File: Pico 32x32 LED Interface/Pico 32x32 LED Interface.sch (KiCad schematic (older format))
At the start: 2 parts, among them J1001 Conn_01x20_Female, U1001 SN74LVC4245APWR

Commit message: Working on things...
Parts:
- removed J1001: Conn_01x20_Female, Connector_PinHeader_2.54mm:PinHeader_1x20_P2.54mm_Vertical, symbol Connector:Conn_01x20_Female
- added C1001, C1002: 100n, Capacitor_SMD:C_0402_1005Metric, symbol Device:C
- added J1002: Conn_02x08_Odd_Even, Connector_PinHeader_2.54mm:PinHeader_2x08_P2.54mm_Vertical, symbol Connector_Generic:Conn_02x08_Odd_Even
- added U?: Pico_Header, symbol LevelShifter:Pico_Header
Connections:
- net +5V: now reaches U1001.1 (VCCA)
- net +5V: now also C1001.1
- net GND: now reaches U1001.11 (GND)
- net GND: now also U1001.12 (GND), U1001.13 (GND), U1001.2 (DIR), U1001.22 (~OE), C1001.2, C1002.1, J1002.16 (Pin_16), J1002.4 (Pin_4), J1002.8 (Pin_8)
- net +3V3: now reaches U1001.23 (VCCB)
- net +3V3: now also U1001.24 (VCCB), C1002.2
- new net AOut: J1002.9 (Pin_9)
- new net B1Out: J1002.3 (Pin_3)
- new net B2Out: J1002.7 (Pin_7)
- new net BOut: J1002.10 (Pin_10)
- new net CLK: J1002.13 (Pin_13)
- new net COut: J1002.11 (Pin_11)
- new net DOut: J1002.12 (Pin_12)
- new net G1Out: J1002.2 (Pin_2)
- new net G2Out: J1002.6 (Pin_6)
- new net LatchOut: J1002.14 (Pin_14)
- new net R1Out: J1002.1 (Pin_1)
- new net R2Out: J1002.5 (Pin_5)
- new net ~OEOut: J1002.15 (Pin_15)

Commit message: Finishing draft
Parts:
- added C2, C4: 100n, Capacitor_SMD:C_0402_1005Metric, symbol Device:C
- added U2: SN74LVC4245APWR, Package_SO:TSSOP-24_6.1x7.8mm_P0.65mm, symbol LevelShifter:SN74LVC4245APWR
- U3: renamed from U?; footprint (none) -> Pico 32x32 LED Interface:Pico_In_Headers
- renumbered C1001 to C1, C1002 to C3, J1002 to J1, U1001 to U1
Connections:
- net CLK is gone; now on net CLKOut: J1.13 (Pin_13)
- net +3V3: now also U3.36 (3V3), C4.2, U2.23 (VCCB), U2.24 (VCCB)
- net +5V: now also U3.40 (VBUS), C2.1, U2.1 (VCCA)
- net AOut: now also U2.6 (A4)
- net B1Out: now also U1.7 (A5)
- net B2Out: now also U1.5 (A3)
- net BOut: now also U2.5 (A3)
- net COut: now also U2.8 (A6)
- net DOut: now also U2.7 (A5)
- net G1Out: now also U1.9 (A7)
- net G2Out: now also U1.10 (A8)
- net GND: now also U3.13 (GND), U3.18 (GND), U3.23 (GND), U3.28 (GND), U3.3 (GND), U3.33 (GND), U3.38 (GND), U3.8 (GND), C2.2, C4.1, U2.11 (GND), U2.12 (GND), U2.13 (GND), U2.14 (B8), U2.15 (B7), U2.2 (DIR), U2.21 (B1), U2.22 (~OE)
- net LatchOut: now also U1.4 (A2)
- net R1Out: now also U1.8 (A6)
- net R2Out: now also U1.6 (A4)
- net ~OEOut: now also U2.4 (A2)
- net at U3.1 (GP0): now also U1.21 (B1)
- net at U3.10 (GP7): now also U1.14 (B8)
- net at U3.11 (GP8): now also U2.20 (B2)
- net at U3.12 (GP9): now also U2.19 (B3)
- net at U3.14 (GP10): now also U2.18 (B4)
- net at U3.15 (GP11): now also U2.17 (B5)
- net at U3.16 (GP12): now also U2.16 (B6)
- net at U3.2 (GP1): now also U1.20 (B2)
- net at U3.4 (GP2): now also U1.19 (B3)
- net at U3.5 (GP3): now also U1.18 (B4)
- net at U3.6 (GP4): now also U1.17 (B5)
- net at U3.7 (GP5): now also U1.16 (B6)
- net at U3.9 (GP6): now also U1.15 (B7)
- net CLKOut: now reaches U1.3 (A1)
- no-connect marks 0 -> 20
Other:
- moved on the sheet: C1, C3, U1, U3

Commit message: Fixing TSSOP footprints (#9)
Fixes the footprints of the TSSOP packages, after JLCPCB caught the error.

Since order, I've noticed two more issues:
- The decoupling capacitors may need larger footprints too (there was a warning about them, but JLCPCB didn't message me like they did for the TSSOP footprints)
- The pinout from the Pico needs to change. I've been learning about the differences between `out`, `set` and `sideset` pins since the order went into production
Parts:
- U1, U2: footprint Package_SO:TSSOP-24_6.1x7.8mm_P0.65mm -> Package_SO:TSSOP-24_4.4x7.8mm_P0.65mm
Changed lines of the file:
@@
 F 0 "U1" H 4900 3855 50  0000 C CNN
 F 1 "SN74LVC4245APWR" H 4900 3764 50  0000 C CNN
-F 2 "Package_SO:TSSOP-24_6.1x7.8mm_P0.65mm" H 4900 2750 50  0001 C CNN
+F 2 "Package_SO:TSSOP-24_4.4x7.8mm_P0.65mm" H 4900 2750 50  0001 C CNN
 F 3 "https://datasheet.lcsc.com/lcsc/1809192324_Texas-Instruments-SN74LVC4245APWR_C7859.pdf" H 4900 2750 50  0001 C CNN
 F 4 "C7859" H 4900 3673 50  0000 C CNN "LCSC"
@@
 F 0 "U2" H 4900 6505 50  0000 C CNN
 F 1 "SN74LVC4245APWR" H 4900 6414 50  0000 C CNN
-F 2 "Package_SO:TSSOP-24_6.1x7.8mm_P0.65mm" H 4900 5400 50  0001 C CNN
+F 2 "Package_SO:TSSOP-24_4.4x7.8mm_P0.65mm" H 4900 5400 50  0001 C CNN
 F 3 "https://datasheet.lcsc.com/lcsc/1809192324_Texas-Instruments-SN74LVC4245APWR_C7859.pdf" H 4900 5400 50  0001 C CNN
 F 4 "C7859" H 4900 6323 50  0000 C CNN "LCSC"

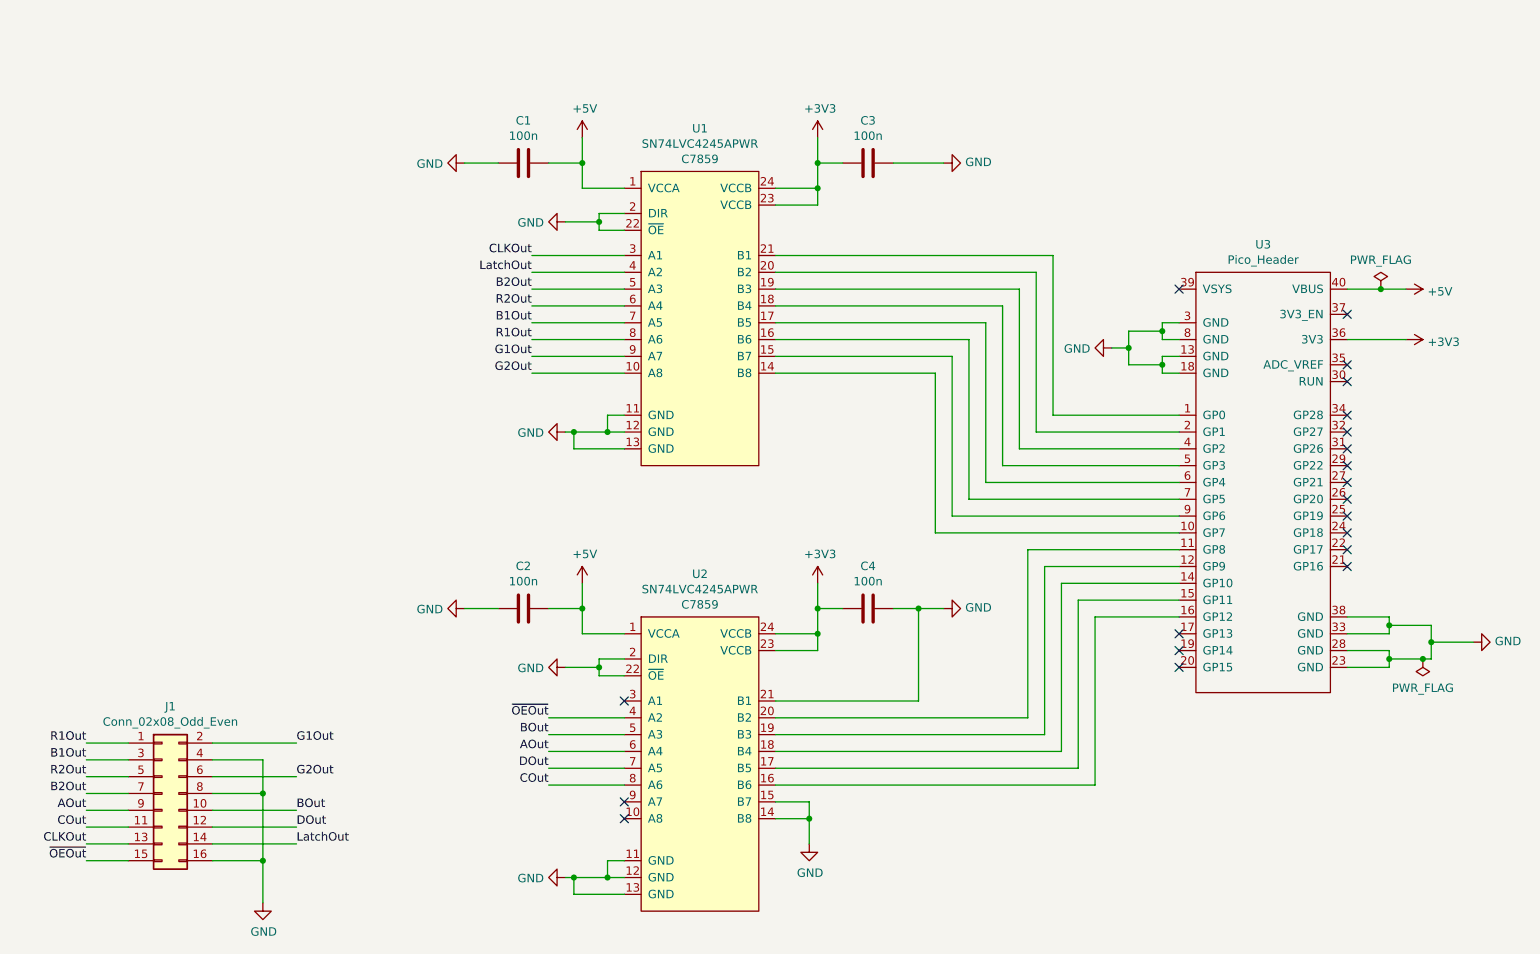
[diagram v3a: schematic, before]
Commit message: Working on reordering connections
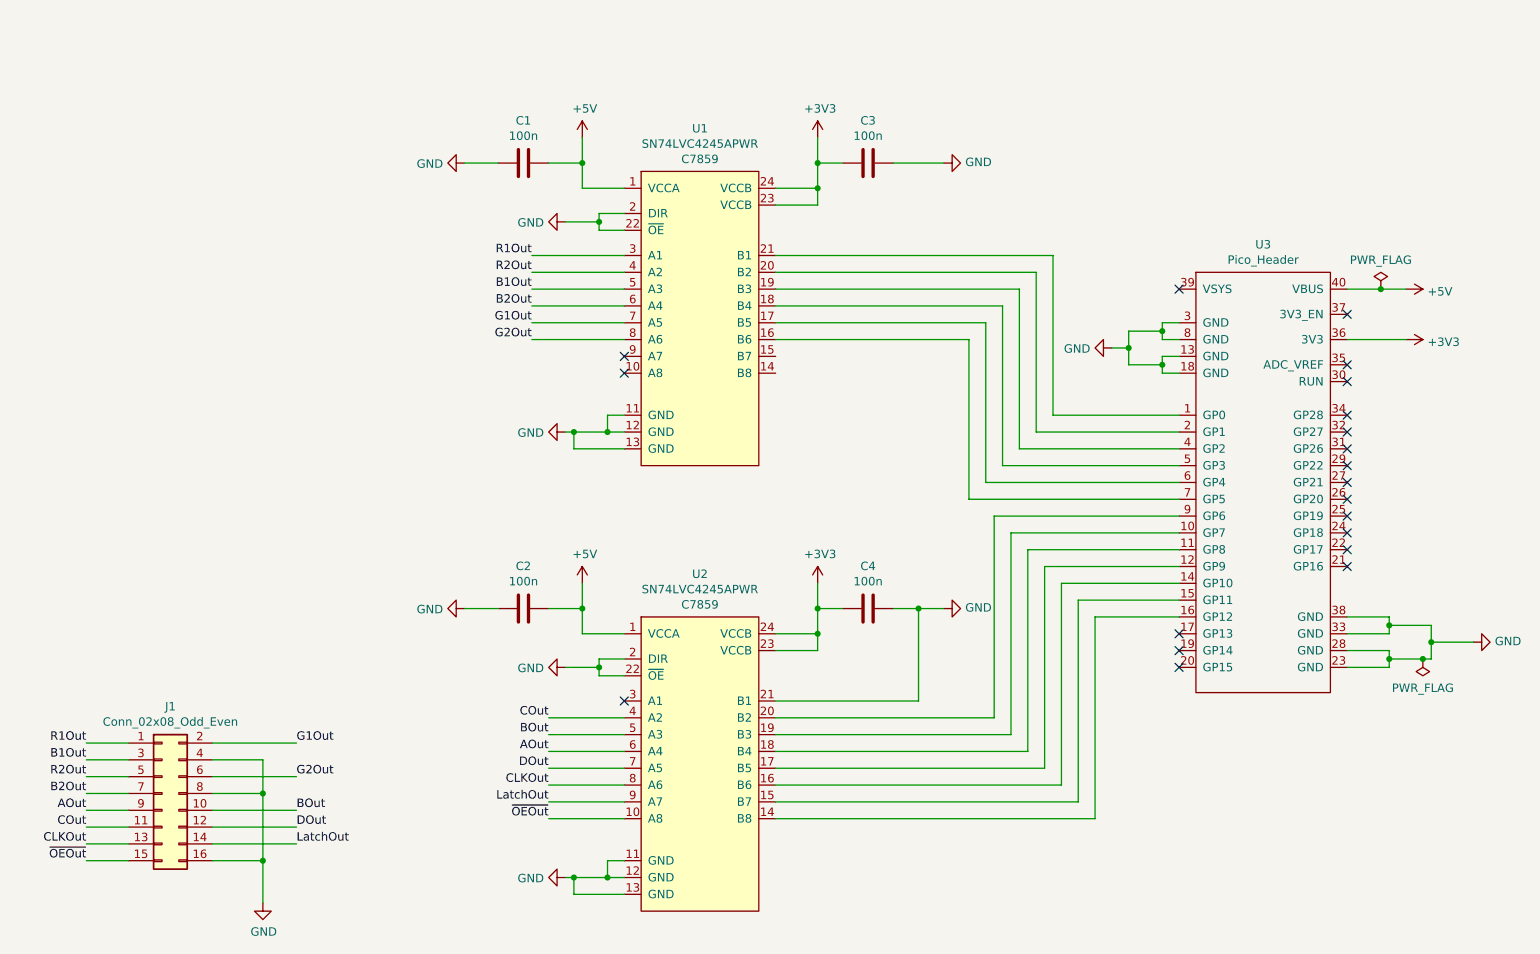
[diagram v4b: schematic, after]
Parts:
- C2, C4: footprint Capacitor_SMD:C_0402_1005Metric -> Capacitor_SMD:C_0402_1005Metric_Pad0.74x0.62mm_HandSolder
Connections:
- net B1Out: now also U1.5 (A3); no longer U1.7 (A5)
- net B2Out: now also U1.6 (A4); no longer U1.5 (A3)
- net CLKOut: now also U2.8 (A6); no longer U1.3 (A1)
- net COut: now also U2.4 (A2); no longer U2.8 (A6)
- net G1Out: now also U1.7 (A5); no longer U1.9 (A7)
- net G2Out: now also U1.8 (A6); no longer U1.10 (A8)
- net GND: no longer U2.14 (B8), U2.15 (B7)
- net LatchOut: now also U2.9 (A7); no longer U1.4 (A2)
- net R1Out: now also U1.3 (A1); no longer U1.8 (A6)
- net R2Out: now also U1.4 (A2); no longer U1.6 (A4)
- net ~OEOut: now also U2.10 (A8); no longer U2.4 (A2)
- net at U3.10 (GP7): now also U2.19 (B3); no longer U1.14 (B8)
- net at U3.11 (GP8): now also U2.18 (B4); no longer U2.20 (B2)
- net at U3.12 (GP9): now also U2.17 (B5); no longer U2.19 (B3)
- net at U3.14 (GP10): now also U2.16 (B6); no longer U2.18 (B4)
- net at U3.15 (GP11): now also U2.15 (B7); no longer U2.17 (B5)
- net at U3.16 (GP12): now also U2.14 (B8); no longer U2.16 (B6)
- net at U3.9 (GP6): now also U2.20 (B2); no longer U1.15 (B7)
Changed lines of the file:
@@
 F 0 "C2" V 3598 4500 50  0000 C CNN
 F 1 "100n" V 3689 4500 50  0000 C CNN
-F 2 "Capacitor_SMD:C_0402_1005Metric" H 3888 4350 50  0001 C CNN
+F 2 "Capacitor_SMD:C_0402_1005Metric_Pad0.74x0.62mm_HandSolder" H 3888 4350 50  0001 C CNN
 F 3 "~" H 3850 4500 50  0001 C CNN
 F 4 "C1525" H 3850 4500 50  0001 C CNN "LCSC"
@@
 F 0 "C4" V 5648 4500 50  0000 C CNN
 F 1 "100n" V 5739 4500 50  0000 C CNN
-F 2 "Capacitor_SMD:C_0402_1005Metric" H 5938 4350 50  0001 C CNN
+F 2 "Capacitor_SMD:C_0402_1005Metric_Pad0.74x0.62mm_HandSolder" H 5938 4350 50  0001 C CNN
 F 3 "~" H 5900 4500 50  0001 C CNN
 F 4 "C1525" H 5900 4500 50  0001 C CNN "LCSC"
@@
 Wire Wire Line
 	6500 3850 7750 3850
-Wire Wire Line
-	5350 3000 6400 3000
-Wire Wire Line
-	6400 3000 6400 3950
-Wire Wire Line
-	6400 3950 7750 3950
 Text Label 3900 2400 2    50   ~ 0
-CLKOut
+R1Out
 Wire Wire Line
 	3900 2400 4450 2400
 Wire Wire Line
-	5350 5150 6850 5150
-Wire Wire Line
-	6850 5150 6850 4150
-Wire Wire Line
 	6850 4150 7750 4150
 Wire Wire Line
-	5350 5250 6950 5250
-Wire Wire Line
-	6950 5250 6950 4250
-Wire Wire Line
 	6950 4250 7750 4250
 Wire Wire Line
-	5350 5350 7050 5350
-Wire Wire Line
-	7050 5350 7050 4350
-Wire Wire Line
 	7050 4350 7750 4350
 Wire Wire Line
 	7750 4450 7150 4450
 Wire Wire Line
-	7150 4450 7150 5450
-Wire Wire Line
-	7150 5450 5350 5450
-Wire Wire Line
-	5350 5550 7250 5550
-Wire Wire Line
-	7250 5550 7250 4550
-Wire Wire Line
 	7250 4550 7750 4550
-$Comp
-L power:GND #PWR0101
-U 1 1 619DC3E4
-P 5550 5900
-F 0 "#PWR0101" H 5550 5650 50  0001 C CNN
-F 1 "GND" H 5555 5727 50  0000 C CNN
-F 2 "" H 5550 5900 50  0001 C CNN
-F 3 "" H 5550 5900 50  0001 C CNN
-	1    5550 5900
-	1    0    0    -1
-$EndComp
-Wire Wire Line
-	5350 5650 5550 5650
-Wire Wire Line
-	5550 5650 5550 5750
-Connection ~ 5550 5750
-Wire Wire Line
-	5550 5750 5550 5900
-Wire Wire Line
-	5350 5750 5550 5750
 Text Label 3900 2500 2    50   ~ 0
-LatchOut
+R2Out
 Wire Wire Line
 	3900 2500 4450 2500
 Text Label 3900 2600 2    50   ~ 0
-B2Out
+B1Out
 Wire Wire Line
 	3900 2600 4450 2600
 Text Label 3900 2700 2    50   ~ 0
-R2Out
+B2Out
 Text Label 3900 2800 2    50   ~ 0
-B1Out
+G1Out
 Wire Wire Line
 	3900 2700 4450 2700
 Wire Wire Line
 	3900 2800 4450 2800
-Wire Wire Line
-	6300 3100 6300 4050
-Wire Wire Line
-	6300 4050 7750 4050
-Wire Wire Line
-	5350 3100 6300 3100
 Wire Wire Line
 	5350 5050 6200 5050
@@
 	6200 4500 6350 4500
 Text Label 3900 2900 2    50   ~ 0
-R1Out
-Text Label 3900 3000 2    50   ~ 0
-G1Out
-Text Label 3900 3100 2    50   ~ 0
 G2Out
 Wire Wire Line
 	3900 2900 4450 2900
-Wire Wire Line
-	3900 3000 4450 3000
-Wire Wire Line
-	3900 3100 4450 3100
-NoConn ~ 4450 5650
-NoConn ~ 4450 5750
-NoConn ~ 4450 5050
 Text Label 4000 5250 2    50   ~ 0
 BOut
@@
 DOut
 Text Label 4000 5550 2    50   ~ 0
+CLKOut
+Text Label 4000 5150 2    50   ~ 0
 COut
-Text Label 4000 5150 2    50   ~ 0
-~OEOut
 Wire Wire Line
 	4000 5150 4450 5150
@@
 Wire Wire Line
 	8950 2600 9100 2600
+NoConn ~ 4450 3000
+NoConn ~ 4450 3100
+Wire Wire Line
+	7750 4050 6750 4050
+Wire Wire Line
+	7750 3950 6650 3950
+Wire Wire Line
+	6650 3950 6650 5150
+Wire Wire Line
+	6650 5150 5350 5150
+Wire Wire Line
+	6750 4050 6750 5250
+Wire Wire Line
+	6750 5250 5350 5250
+Wire Wire Line
+	6850 4150 6850 5350
+Wire Wire Line
+	6850 5350 5350 5350
+Wire Wire Line
+	6950 4250 6950 5450
+Wire Wire Line
+	6950 5450 5350 5450
+Wire Wire Line
+	7050 4350 7050 5550
+Wire Wire Line
+	7050 5550 5350 5550
+Wire Wire Line
+	7150 4450 7150 5650
+Wire Wire Line
+	7150 5650 5350 5650
+Wire Wire Line
+	7250 4550 7250 5750
+Wire Wire Line
+	7250 5750 5350 5750
+Wire Wire Line
+	4450 5650 4000 5650
+Wire Wire Line
+	4450 5750 4000 5750
+Text Label 4000 5750 2    50   ~ 0
+~OEOut
+Text Label 4000 5650 2    50   ~ 0
+LatchOut
+NoConn ~ 4450 5050
 $EndSCHEMATC

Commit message: Some more routine
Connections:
- net CLKOut: now also U2.10 (A8); no longer U2.8 (A6)
- net GND: now also U1.14 (B8), U1.15 (B7)
- net LatchOut: now also U2.8 (A6); no longer U2.9 (A7)
- net ~OEOut: now also U2.9 (A7); no longer U2.10 (A8)
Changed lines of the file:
@@
 DOut
 Text Label 4000 5550 2    50   ~ 0
-CLKOut
+LatchOut
 Text Label 4000 5150 2    50   ~ 0
 COut
@@
 	4450 5750 4000 5750
 Text Label 4000 5750 2    50   ~ 0
+CLKOut
+Text Label 4000 5650 2    50   ~ 0
 ~OEOut
-Text Label 4000 5650 2    50   ~ 0
-LatchOut
 NoConn ~ 4450 5050
+$Comp
+L power:GND #PWR0101
+U 1 1 61BDDFEA
+P 5550 3350
+F 0 "#PWR0101" H 5550 3100 50  0001 C CNN
+F 1 "GND" H 5555 3177 50  0000 C CNN
+F 2 "" H 5550 3350 50  0001 C CNN
+F 3 "" H 5550 3350 50  0001 C CNN
+	1    5550 3350
+	1    0    0    -1
+$EndComp
+Wire Wire Line
+	5350 3000 5550 3000
+Wire Wire Line
+	5550 3000 5550 3100
+Wire Wire Line
+	5350 3100 5550 3100
+Connection ~ 5550 3100
+Wire Wire Line
+	5550 3100 5550 3350
 $EndSCHEMATC

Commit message: Rethinking sideset pins slightly
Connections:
- net LatchOut: now also U2.9 (A7); no longer U2.8 (A6)
- net ~OEOut: now also U2.8 (A6); no longer U2.9 (A7)
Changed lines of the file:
@@
 DOut
 Text Label 4000 5550 2    50   ~ 0
-LatchOut
+~OEOut
 Text Label 4000 5150 2    50   ~ 0
 COut
@@
 CLKOut
 Text Label 4000 5650 2    50   ~ 0
-~OEOut
+LatchOut
 NoConn ~ 4450 5050
 $Comp
